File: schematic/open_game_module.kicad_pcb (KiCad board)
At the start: 2 copper layers, 78.3 x 49 mm, 18 parts, among them J1 Expansion Port, J2 Conn_02x05_Odd_Even, U1 EPM7064S, U2 YMZ284, U3 HM62256BLP

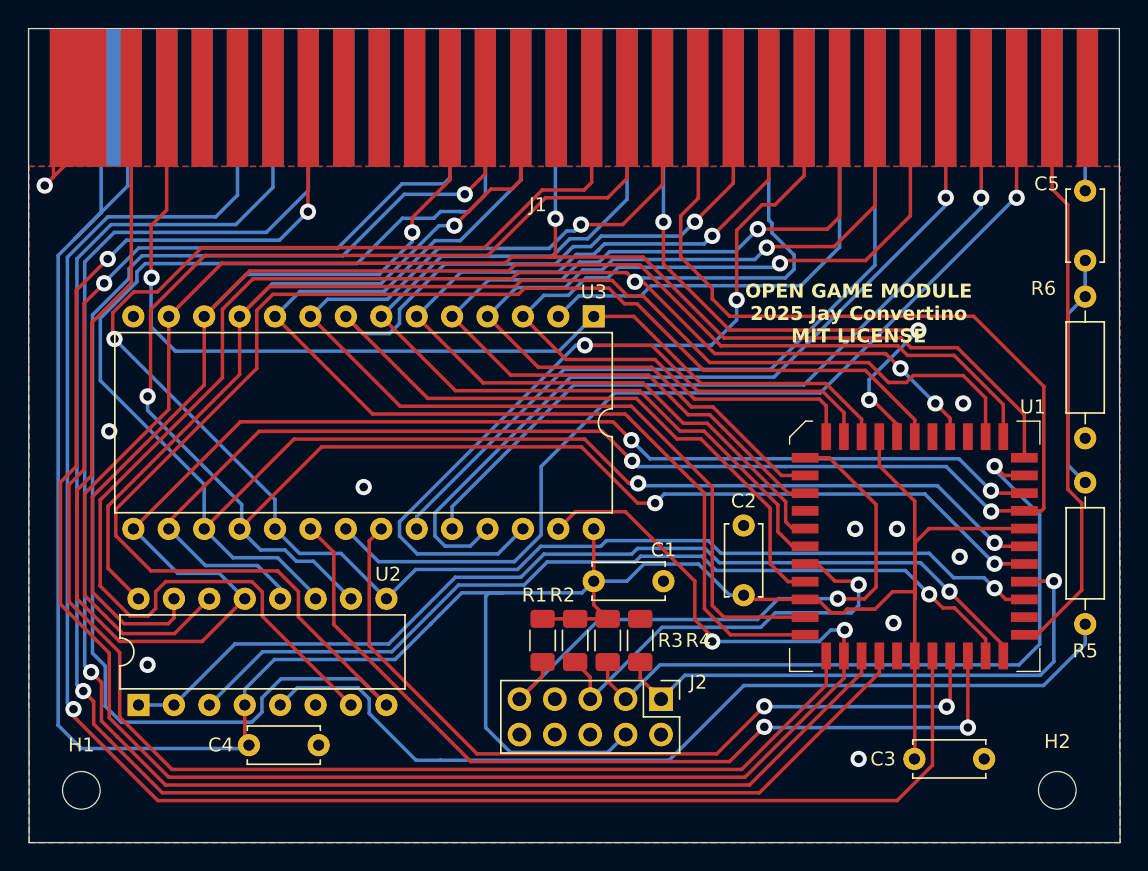
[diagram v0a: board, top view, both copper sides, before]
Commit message: added models and pof from quartus
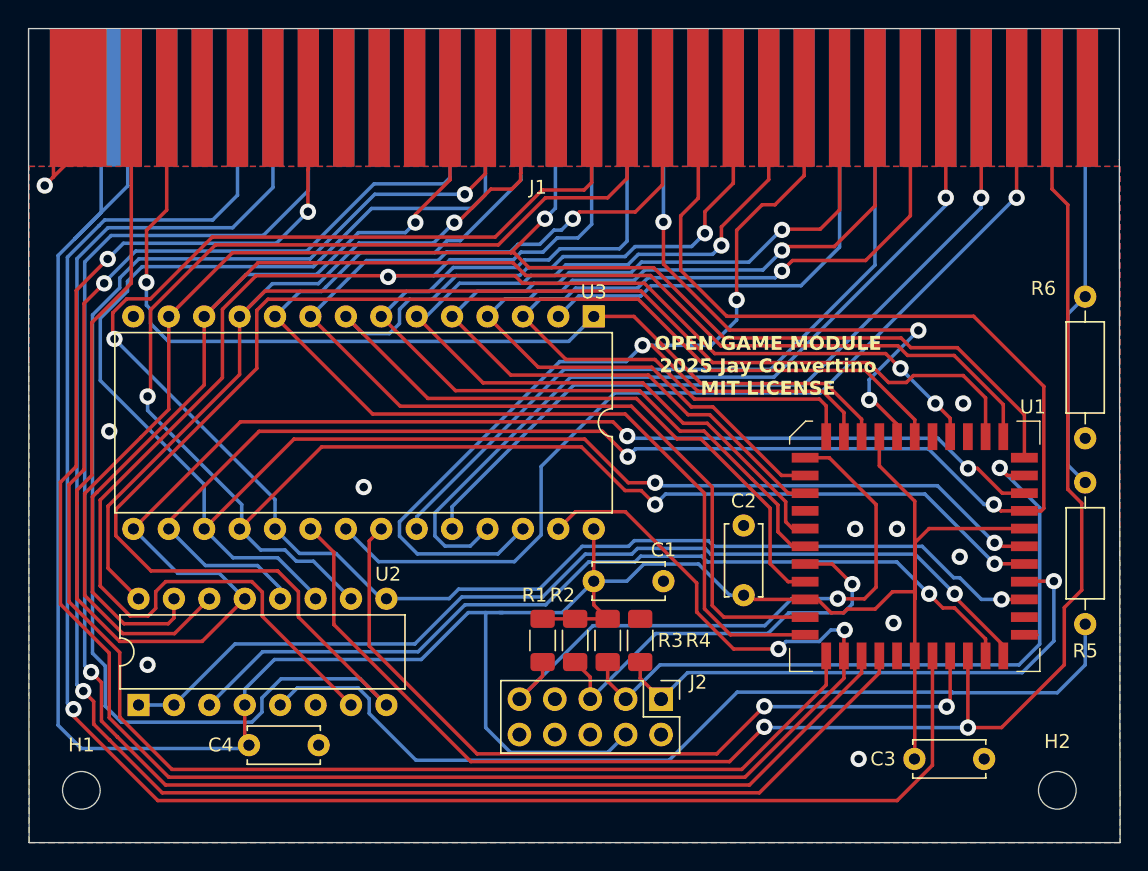
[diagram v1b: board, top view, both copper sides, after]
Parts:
- removed C5: 100nF, Capacitor_THT:C_Disc_D5.0mm_W2.5mm_P5.00mm
- R5: value 1k -> 470R
- R6: value 1k -> 4k7
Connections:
- J1 pad 29: /DIS_MEM -> /~{RAM_CS}
- J1 pad 40: /~{CLK} -> unconnected-(J1-Pin_40-Pad40)
- J1 pad 45: unconnected-(J1-Pin_45-Pad45) -> /~{CLK}
- R5 pad 1: Net-(C5-Pad2) -> Net-(J1-Pin_31)
- R6 pad 2: Net-(C5-Pad2) -> Net-(J1-Pin_31)
- U1 pad 29: /DIS_MEM -> unconnected-(U1-I/O-Pad29)
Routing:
- net /~{RAM_CS}: track 63.3 -> 114.2 mm
- net /DIS_MEM: track 41.6 -> 0.00 mm
- net Net-(J1-Pin_31): track 6.75 -> 28.7 mm
- net Net-(C5-Pad2): track 16.9 -> 0.00 mm
- net /A13: track 82.1 -> 78.0 mm
- net +5V: track 200.5 -> 198.3 mm
- net /A3: track 66.8 -> 68.5 mm
- net /TMS: track 31.1 -> 30.1 mm
- net Net-(U2-OUT): track 65.9 -> 66.8 mm
- net /A2: track 82.7 -> 83.6 mm
- net unconnected-(U1-I/O-Pad29): track 0.00 -> 0.91 mm
- net /TCK: track 40.5 -> 39.6 mm
- net /D4: track 130.0 -> 130.8 mm
- net /A4: track 70.2 -> 71.0 mm
- net /D2: track 117.2 -> 118.0 mm
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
